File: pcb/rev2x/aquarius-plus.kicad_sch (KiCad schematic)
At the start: 216 parts, among them J1 Cassette in, J10 Audio out, J11 Hand controller 2, J12 ESP USB Host, J13 Power in, J14 FPGA spare, J15 Expansion port, J16 ESP32 spare, J2 Cassette out, J3 Amphenol GSD090012SEU, J4 Printer, J5 Hand controller 1, J6 VGA, J7 DBG, J8 USB_A, J9 USB_A, Q1 BC847C, Q2 BC847C, SW1 SW_DPDT_x2, U1 XC3S200-4TQG144, U10 IS61C5128AS-25QLI, U11 74LVC4245APW, U12 74HC166, U13 SST39SF020A-55-4C-WHE, U14 74LVC4245APW, U15 LDL1117S33R, U16 MCP1700T-2502E/TT, U17 LD1117S12, U2 SN74CBTD3861PWR, U3 MAX3221ECPWR, U4 SN74CBTD3861PWR, U5 ESP32-S2-SOLO-N4R2, U6 SN74CBTD3861PWR, U7 Z84C0010AEG, U8 SN74CBTD3861PWR, U9 74HC166, X1 ECS-5032MV-143-CN-TR, X2 ECS-5032MV-480-BN-TR

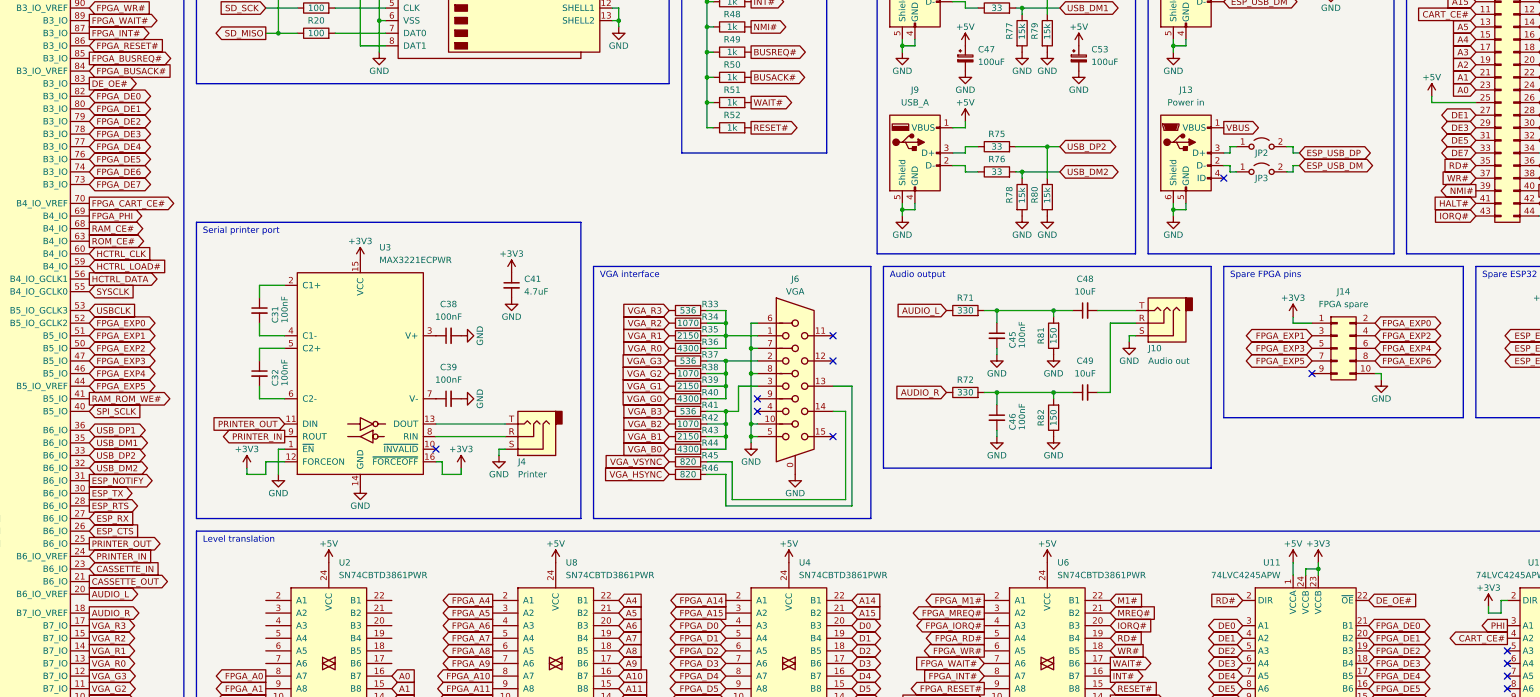
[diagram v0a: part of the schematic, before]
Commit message: Further U11 & U14 Updates
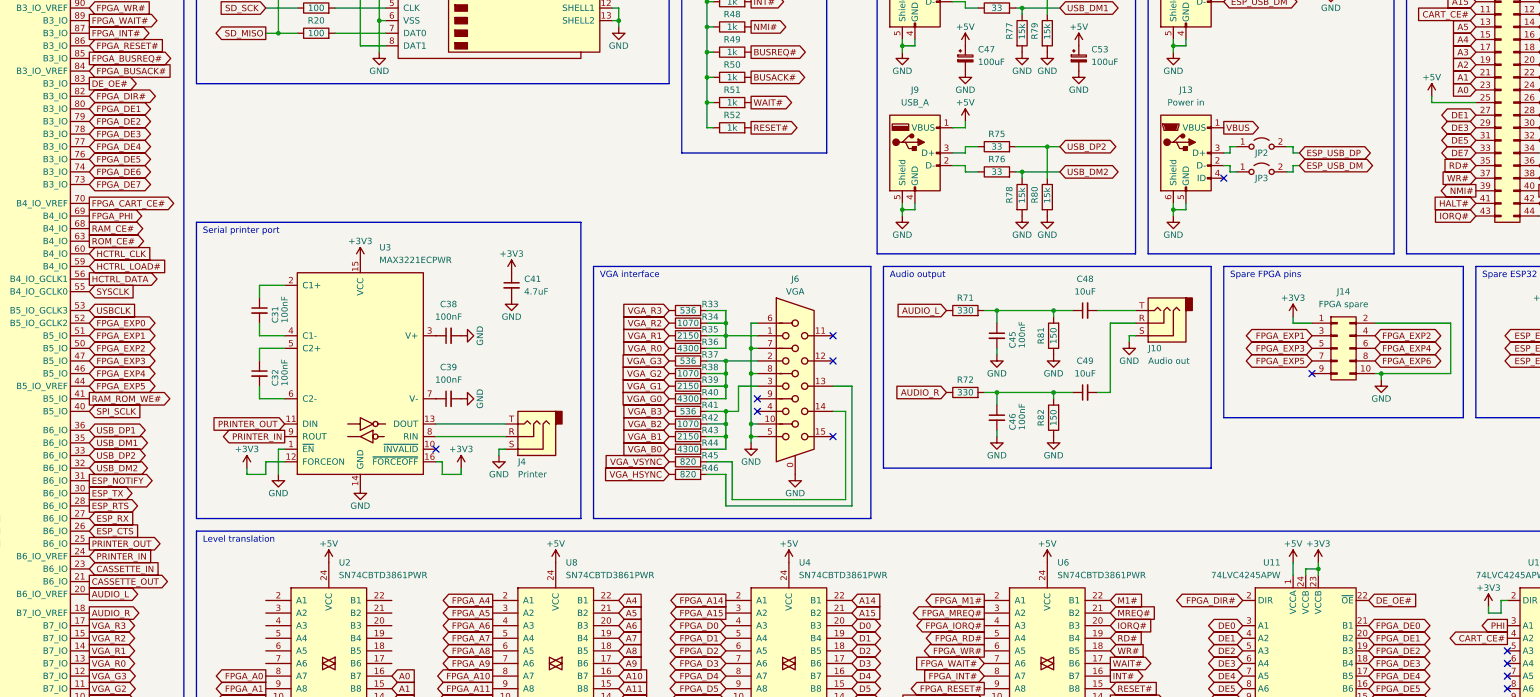
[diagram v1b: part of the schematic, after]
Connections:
- net FPGA_DE0: no longer U1.82 (B3_IO)
- net FPGA_EXP0: no longer J14.2 (Pin_2)
- net GND: now also J14.2 (Pin_2)
- net RD#: no longer U11.2 (DIR)
- new net FPGA_DIR#: U1.82 (B3_IO), U11.2 (DIR)
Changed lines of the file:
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@@
   (title_block
     (title "Aquarius+")
-    (date "2023-03-02")
+    (date "2023-03-05")
     (rev "2x")
     (company "Designed by Frank van den Hoef")
@@
   (junction (at 461.01 63.5) (diameter 0) (color 0 0 0 0)
   )
+  (junction (at 341.63 191.77) (diameter 0) (color 0 0 0 0)
+  )
   (junction (at 24.13 289.56) (diameter 0) (color 0 0 0 0)
   )
@@
     (stroke (width 0) (type default) (color 0 0 0 0))
   )
+  (wire (pts (xy 355.6 181.61) (xy 355.6 191.77))
+    (stroke (width 0) (type default) (color 0 0 0 0))
+  )
   (wire (pts (xy 392.43 247.65) (xy 394.97 247.65))
     (stroke (width 0) (type default) (color 0 0 0 0))
@@
     (stroke (width 0) (type default) (color 0 0 0 0))
   )
+  (wire (pts (xy 341.63 191.77) (xy 355.6 191.77))
+    (stroke (width 0) (type default) (color 0 0 0 0))
+  )
   (wire (pts (xy 421.64 25.4) (xy 422.91 25.4))
     (stroke (width 0) (type default) (color 0 0 0 0))
@@
     (stroke (width 0) (type default) (color 0 0 0 0))
   )
+  (wire (pts (xy 340.36 181.61) (xy 355.6 181.61))
+    (stroke (width 0) (type default) (color 0 0 0 0))
+  )
   (wire (pts (xy 44.45 213.36) (xy 44.45 215.9))
     (stroke (width 0) (type default) (color 0 0 0 0))
@@
     )
   )
-  (global_label "RD#" (shape input) (at 313.69 237.49 180) (fields_autoplaced)
-    (effects (font (size 1.27 1.27)) (justify right))
-    (property "Intersheet References" "${INTERSHEET_REFS}" (id 0) (at 307.4669 237.5694 0)
-      (effects (font (size 1.27 1.27)) (justify right) hide)
-    )
-  )
   (global_label "USBCLK" (shape input) (at 81.28 179.07 0) (fields_autoplaced)
     (effects (font (size 1.27 1.27)) (justify left))
@@
     )
   )
-  (global_label "FPGA_DE0" (shape bidirectional) (at 81.28 135.89 0) (fields_autoplaced)
+  (global_label "FPGA_DIR#" (shape bidirectional) (at 81.28 135.89 0) (fields_autoplaced)
     (effects (font (size 1.27 1.27)) (justify left))
-    (property "Intersheet References" "${INTERSHEET_REFS}" (id 0) (at 93.0064 135.8106 0)
+    (property "Intersheet References" "${INTERSHEET_REFS}" (id 0) (at 93.7926 135.8106 0)
       (effects (font (size 1.27 1.27)) (justify left) hide)
     )
@@
     )
   )
-  (global_label "FPGA_EXP0" (shape bidirectional) (at 340.36 181.61 0) (fields_autoplaced)
-    (effects (font (size 1.27 1.27)) (justify left))
-    (property "Intersheet References" "${INTERSHEET_REFS}" (id 0) (at 353.296 181.5306 0)
-      (effects (font (size 1.27 1.27)) (justify left) hide)
-    )
-  )
   (global_label "A6" (shape input) (at 187.96 242.57 0) (fields_autoplaced)
     (effects (font (size 1.27 1.27)) (justify left))
@@
     )
   )
+  (global_label "FPGA_DIR#" (shape bidirectional) (at 313.69 237.49 180) (fields_autoplaced)
+    (effects (font (size 1.27 1.27)) (justify right))
+    (property "Intersheet References" "${INTERSHEET_REFS}" (id 0) (at 301.1774 237.4106 0)
+      (effects (font (size 1.27 1.27)) (justify right) hide)
+    )
+  )
   (global_label "WR#" (shape input) (at 360.68 152.4 180) (fields_autoplaced)
     (effects (font (size 1.27 1.27)) (justify right))
@@
   (symbol (lib_id "power:GND") (at 377.19 193.04 0) (unit 1)
     (in_bom yes) (on_board yes)
-    (property "Reference" "#PWR?" (id 0) (at 377.19 199.39 0)
+    (property "Reference" "#PWR0132" (id 0) (at 377.19 199.39 0)
       (effects (font (size 1.27 1.27)) hide)
     )
@@
   (symbol (lib_id "power:+5V") (at 323.85 229.87 0) (unit 1)
     (in_bom yes) (on_board yes)
-    (property "Reference" "#PWR?" (id 0) (at 323.85 233.68 0)
+    (property "Reference" "#PWR0153" (id 0) (at 323.85 233.68 0)
       (effects (font (size 1.27 1.27)) hide)
     )
@@
   (symbol (lib_id "power:GND") (at 398.78 248.92 0) (mirror y) (unit 1)
     (in_bom yes) (on_board yes)
-    (property "Reference" "#PWR?" (id 0) (at 398.78 255.27 0)
+    (property "Reference" "#PWR0126" (id 0) (at 398.78 255.27 0)
       (effects (font (size 1.27 1.27)) hide)
     )
@@
   (symbol (lib_id "power:+5V") (at 377.19 229.87 0) (mirror y) (unit 1)
     (in_bom yes) (on_board yes)
-    (property "Reference" "#PWR?" (id 0) (at 377.19 233.68 0)
+    (property "Reference" "#PWR0179" (id 0) (at 377.19 233.68 0)
       (effects (font (size 1.27 1.27)) hide)
     )
@@
   (symbol (lib_id "power:+3V3") (at 328.93 229.87 0) (unit 1)
     (in_bom yes) (on_board yes)
-    (property "Reference" "#PWR?" (id 0) (at 328.93 233.68 0)
+    (property "Reference" "#PWR0150" (id 0) (at 328.93 233.68 0)
       (effects (font (size 1.27 1.27)) hide)
     )
@@
   (symbol (lib_id "power:+3V3") (at 382.27 229.87 0) (mirror y) (unit 1)
     (in_bom yes) (on_board yes)
-    (property "Reference" "#PWR?" (id 0) (at 382.27 233.68 0)
+    (property "Reference" "#PWR0180" (id 0) (at 382.27 233.68 0)
       (effects (font (size 1.27 1.27)) hide)
     )
@@
       (reference "#PWR0125") (unit 1) (value "+3V3") (footprint "")
     )
+    (path "/62a2c375-dd0f-469b-b970-48cafa106995"
+      (reference "#PWR0126") (unit 1) (value "GND") (footprint "")
+    )
     (path "/51c5e032-6740-4d07-84c8-55db32ba884a"
       (reference "#PWR0127") (unit 1) (value "GND") (footprint "")
@@
       (reference "#PWR0131") (unit 1) (value "GND") (footprint "")
     )
+    (path "/04b7b962-218d-46e7-9f31-1a279c45a27c"
+      (reference "#PWR0132") (unit 1) (value "GND") (footprint "")
+    )
     (path "/007e16c6-e036-42fc-b84a-826528d61dec"
       (reference "#PWR0133") (unit 1) (value "+5V") (footprint "")
@@
       (reference "#PWR0149") (unit 1) (value "+3V3") (footprint "")
     )
+    (path "/9a434b45-c5e1-48a5-a4c6-e1f388e90587"
+      (reference "#PWR0150") (unit 1) (value "+3V3") (footprint "")
+    )
     (path "/ae809102-ba02-4cdf-a9ae-78ddde60f12e"
       (reference "#PWR0151") (unit 1) (value "GND") (footprint "")
@@
       (reference "#PWR0152") (unit 1) (value "GND") (footprint "")
     )
+    (path "/5e6f3146-8d81-4d38-9225-40a455fd4f1f"
+      (reference "#PWR0153") (unit 1) (value "+5V") (footprint "")
+    )
     (path "/ba29f725-68bb-414d-bbfe-ef80cc0f10b7"
       (reference "#PWR0154") (unit 1) (value "+5V") (footprint "")
@@
       (reference "#PWR0178") (unit 1) (value "GND") (footprint "")
     )
-    (path "/04b7b962-218d-46e7-9f31-1a279c45a27c"
-      (reference "#PWR?") (unit 1) (value "GND") (footprint "")
-    )
-    (path "/5e6f3146-8d81-4d38-9225-40a455fd4f1f"
-      (reference "#PWR?") (unit 1) (value "+5V") (footprint "")
-    )
-    (path "/62a2c375-dd0f-469b-b970-48cafa106995"
-      (reference "#PWR?") (unit 1) (value "GND") (footprint "")
-    )
     (path "/64738936-cacc-4a67-bc6b-c1c75699a64b"
-      (reference "#PWR?") (unit 1) (value "+5V") (footprint "")
-    )
-    (path "/9a434b45-c5e1-48a5-a4c6-e1f388e90587"
-      (reference "#PWR?") (unit 1) (value "+3V3") (footprint "")
+      (reference "#PWR0179") (unit 1) (value "+5V") (footprint "")
     )
     (path "/b4fdd99e-51b0-469e-af9d-7bba15fb1ec6"
-      (reference "#PWR?") (unit 1) (value "+3V3") (footprint "")
+      (reference "#PWR0180") (unit 1) (value "+3V3") (footprint "")
     )
     (path "/52d4c05f-c0de-4113-8daf-5e4446b453ca"

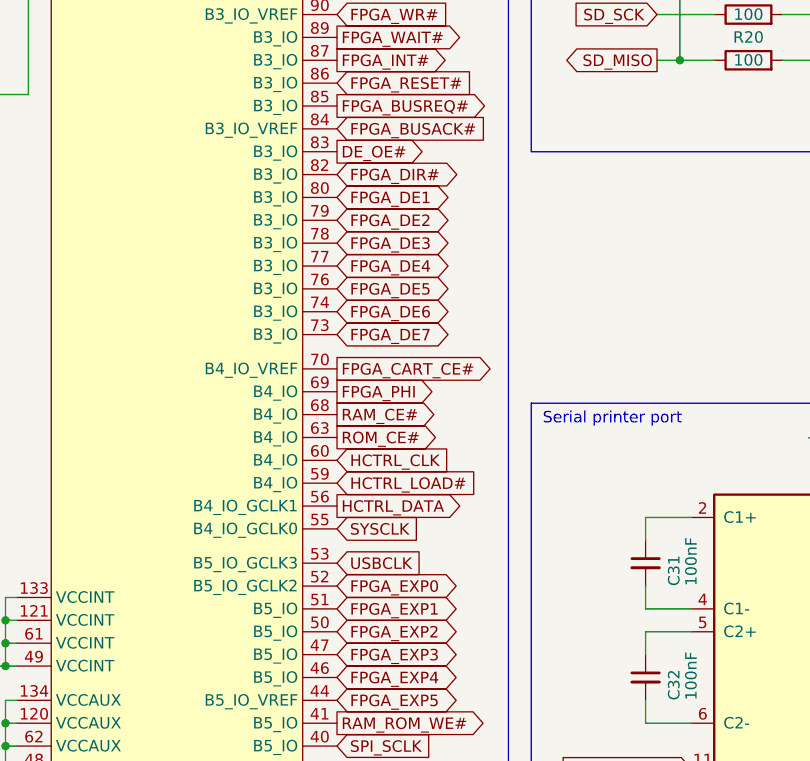
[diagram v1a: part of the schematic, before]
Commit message: Fixed FPGA_DIR# and FPGA_DE0 wiring.
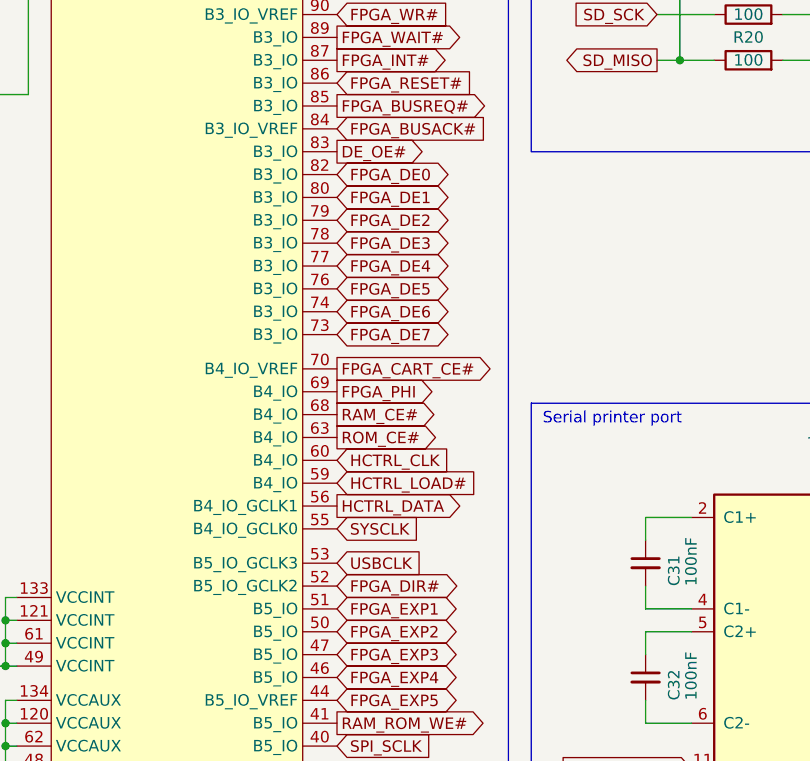
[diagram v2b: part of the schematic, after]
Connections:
- net FPGA_EXP0 is gone; now on net FPGA_DIR#: U1.52 (B5_IO_GCLK2)
- net FPGA_DE0: now also U1.82 (B3_IO)
- net FPGA_DIR#: no longer U1.82 (B3_IO)
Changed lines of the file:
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@@
   (title_block
     (title "Aquarius+")
-    (date "2023-03-05")
+    (date "2023-03-06")
     (rev "2x")
     (company "Designed by Frank van den Hoef")
@@
     )
   )
-  (global_label "FPGA_EXP0" (shape bidirectional) (at 81.28 181.61 0) (fields_autoplaced)
+  (global_label "FPGA_DIR#" (shape bidirectional) (at 81.28 181.61 0) (fields_autoplaced)
     (effects (font (size 1.27 1.27)) (justify left))
-    (property "Intersheet References" "${INTERSHEET_REFS}" (id 0) (at 94.216 181.5306 0)
+    (property "Intersheet References" "${INTERSHEET_REFS}" (id 0) (at 93.7926 181.5306 0)
       (effects (font (size 1.27 1.27)) (justify left) hide)
     )
@@
     )
   )
-  (global_label "FPGA_DIR#" (shape bidirectional) (at 81.28 135.89 0) (fields_autoplaced)
+  (global_label "FPGA_DE0" (shape bidirectional) (at 81.28 135.89 0) (fields_autoplaced)
     (effects (font (size 1.27 1.27)) (justify left))
-    (property "Intersheet References" "${INTERSHEET_REFS}" (id 0) (at 93.7926 135.8106 0)
+    (property "Intersheet References" "${INTERSHEET_REFS}" (id 0) (at 93.0064 135.8106 0)
       (effects (font (size 1.27 1.27)) (justify left) hide)
     )
